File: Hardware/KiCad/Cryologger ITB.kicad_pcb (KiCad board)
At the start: 2 copper layers, 134.6 x 63.5 mm, 18 parts, among them J1 Screw_Terminal_01x02, U1 Adafruit_LSM303AGR, U2 Adafruit_DPS310, U3 Adafruit_Feather_Header, U4 Adafruit_Feather_Header, U5 ROCKBLOCK_9603, U6 Pololu_D36V6, U7 Pololu_D36V6, U8 RockBLOCK_Footprint

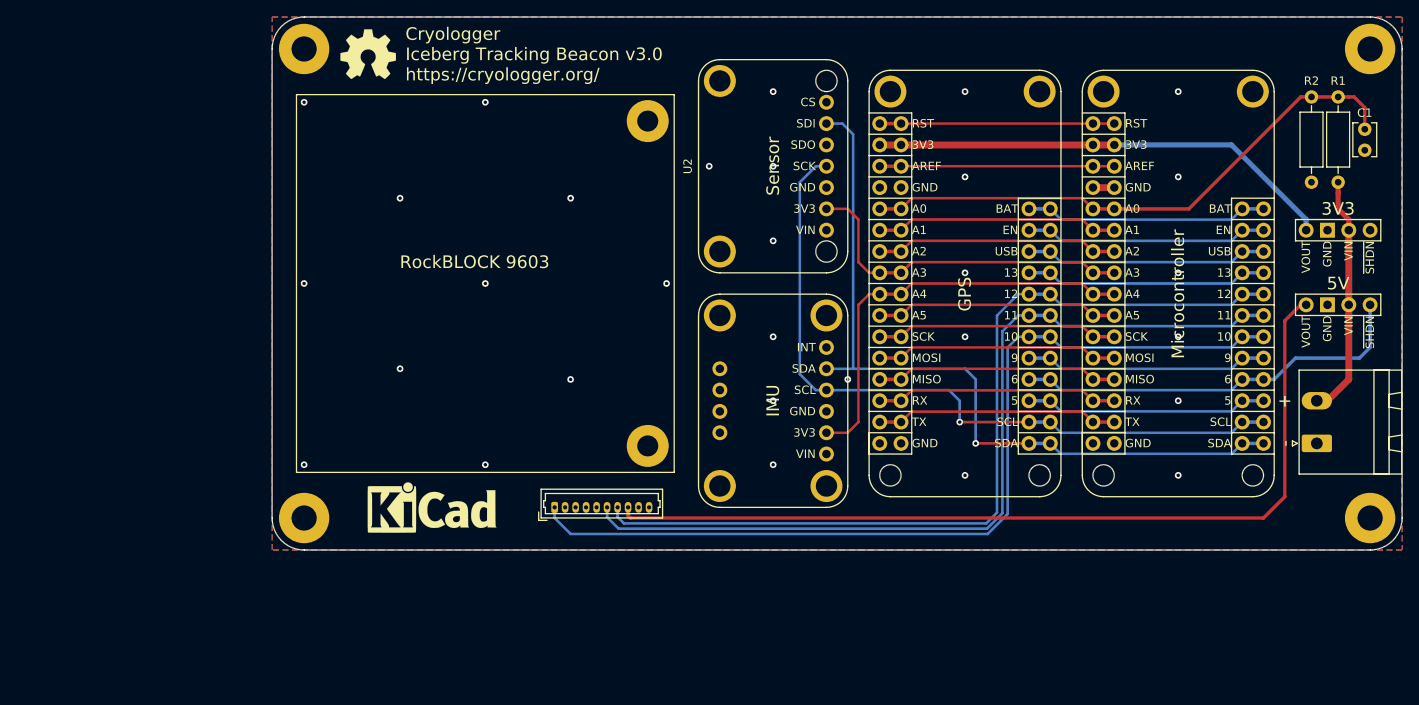
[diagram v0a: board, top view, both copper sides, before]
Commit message: Major changes to KiCad design files
Updated design to v3.1. Began standardization of Cryologger designs to metric measurements. Redid schematic using Cryologger library symbols and footprints. Generated new Gerber design files. Generated current schematic and PCB layout documents. Cleaned up redundant KiCad project files. Removed old 3D printing designs.
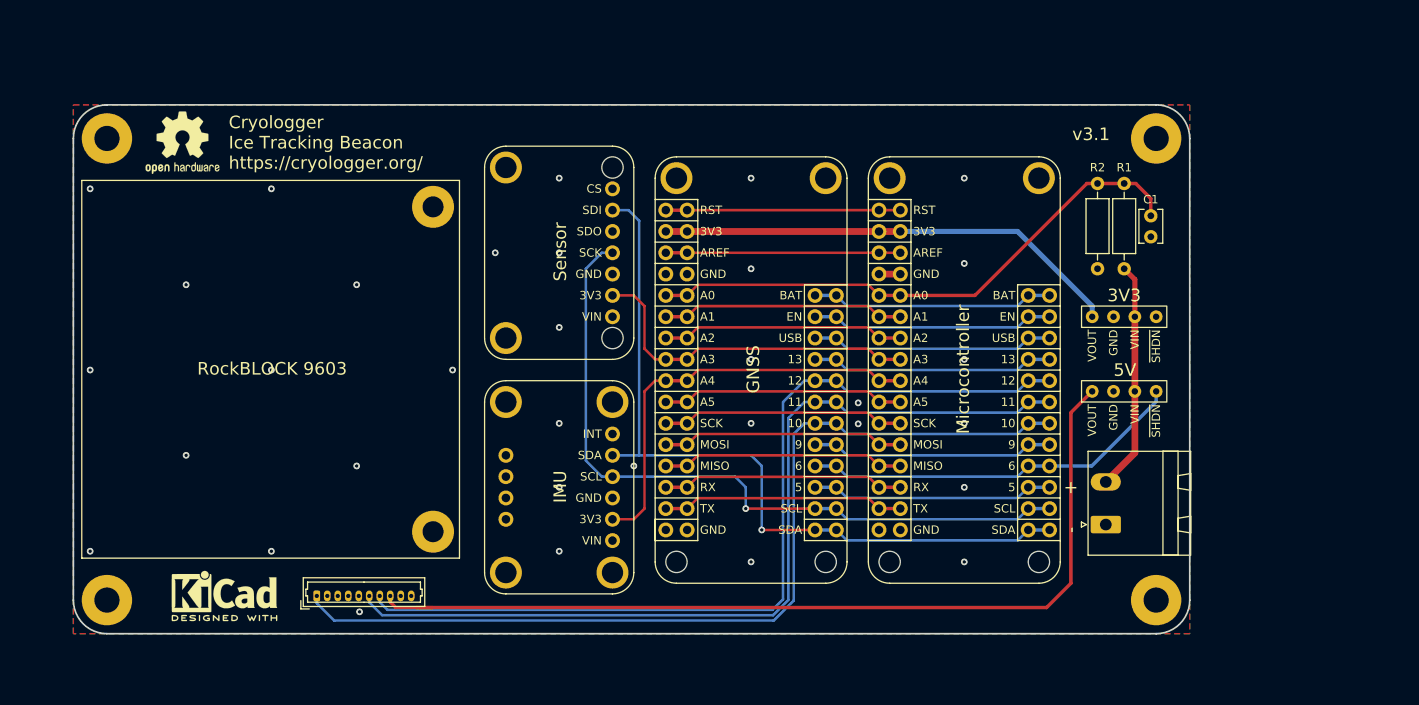
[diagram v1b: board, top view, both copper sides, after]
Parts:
- removed the REF** at (118.1, 54.0)
- removed the REF** at (125.7, 108.0)
- removed U4: Adafruit_Feather_Header, Cryologger:Adafruit_Feather_Header_Double
- removed U5: ROCKBLOCK_9603, Connector_Molex:Molex_PicoBlade_53047-1010_1x10_P1.25mm_Vertical
- removed U7: Pololu_D36V6, Cryologger:Pololu_D36V6_Vertical
- added A2: Adafruit_Feather_Generic, Cryologger:Adafruit_Feather_Header_Double, F.Cu at (163.7, 91.6)
- added A3: Adafruit_Feather_M0_Basic_Proto, Cryologger:Adafruit_Feather_Header_Double, F.Cu at (189.1, 91.6)
- added REF**: OSHW-Logo2_9.8x8mm_SilkScreen, Symbol:OSHW-Logo2_9.8x8mm_SilkScreen, F.Cu at (96.0, 64.5)
- added REF**: KiCad-Logo2_5mm_SilkScreen, Symbol:KiCad-Logo2_5mm_SilkScreen, F.Cu at (101.0, 118.5)
- added U9: Pololu_D36V6x, Cryologger:Pololu_D36V6x, F.Cu at (208.2, 86.5)
- R1: value R_US -> 10MΩ
- R2: value R_US -> 1MΩ
- U2: value Adafruit_DPS310 -> Pololu_D36V6x; footprint Cryologger:Adafruit_DPS310 -> Cryologger:Pololu_D36V6x
- U3: value Adafruit_Feather_Header -> ~; footprint Cryologger:Adafruit_Feather_Header_Double -> Connector_Molex:Molex_PicoBlade_53047-1010_1x10_P1.25mm_Vertical
- U6: value Pololu_D36V6 -> Adafruit_BME280; footprint Cryologger:Pololu_D36V6_Vertical -> Cryologger:Adafruit_DPS310
- U8: footprint Cryologger:RockBLOCK_9603_Footprint -> Cryologger:RockBLOCK_9603
- moved U6 92.8 mm to (140.9, 77.6)
- moved U3 85.7 mm to (112.0, 118.5)
- moved U2 50.4 mm to (208.2, 95.4), turned to 0 degrees
- moved H3 27.6 mm to (212.0, 64.0)
- moved U8 27.5 mm to (106.5, 91.5), turned to 0 degrees
- moved R1 27.5 mm to (208.2, 79.5)
- moved U1 27.5 mm to (140.9, 105.6), turned to 0 degrees
- moved R2 27.5 mm to (205.0, 69.4)
- moved C1 27.5 mm to (211.4, 73.2)
- moved H4 27.3 mm to (212.0, 119.0)
- moved J1 26.9 mm to (206.0, 110.0)
- moved H2 25.8 mm to (87.0, 64.0)
- moved H1 25.4 mm to (87.0, 119.0)
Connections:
- C1 pad 1: /A0 -> A0
- H1 pad 1: GND -> unconnected-(H1-Pad1)
- H2 pad 1: GND -> unconnected-(H2-Pad1)
- H3 pad 1: GND -> unconnected-(H3-Pad1)
- H4 pad 1: GND -> unconnected-(H4-Pad1)
- R1 pad 2: /A0 -> A0
- R2 pad 1: /A0 -> A0
- U1 pad 1: (no net) -> unconnected-(U1-5V-Pad1)
- U1 pad 2: /A4 -> A4
- U1 pad 4: /SCL -> SCL
- U1 pad 5: /SDA -> SDA
- U2 pad 1: (no net) -> +5V
- U2 pad 2: /A3 -> GND
- U2 pad 3: GND -> +BATT
- U2 pad 4: /SCL -> D6
- U3 pad 1: /RST -> D10
- U3 pad 10: /A5 -> GND
- U3 pad 2: +3V3 -> unconnected-(U3-CTS-Pad2)
- U3 pad 3: /AREF -> unconnected-(U3-RTC-Pad3)
- U3 pad 4: GND -> unconnected-(U3-NetAv-Pad4)
- U3 pad 5: /A0 -> unconnected-(U3-RI-Pad5)
- U3 pad 6: /A1 -> D11
- U3 pad 7: /A2 -> D12
- U3 pad 8: /A3 -> +5V
- U3 pad 9: /A4 -> unconnected-(U3-LiIon-Pad9)
- U6 pad 1: +3V3 -> unconnected-(U6-5V-Pad1)
- U6 pad 2: GND -> A3
- U6 pad 3: +BATT -> GND
- U6 pad 4: (no net) -> SCL
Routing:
- net D10: track 0.00 -> 111.4 mm
- net +5V: track 0.00 -> 109.0 mm
- net /D10: track 108.9 -> 0.00 mm
- net D12: track 0.00 -> 107.1 mm
- net D11: track 0.00 -> 106.7 mm
- net /5V: track 105.0 -> 0.00 mm
- net /D12: track 104.5 -> 0.00 mm
- net /D11: track 104.2 -> 0.00 mm
- net /SDA: track 93.5 -> 0.00 mm, vias 1 -> 0
- net SDA: track 0.00 -> 92.9 mm, vias 0 -> 1
- net /SCL: track 87.6 -> 0.00 mm, vias 1 -> 0
- net SCL: track 0.00 -> 87.0 mm, vias 0 -> 1
- net /A0: track 67.4 -> 0.00 mm
- net A0: track 0.00 -> 67.2 mm
- net A4: track 0.00 -> 50.4 mm
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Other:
- board size 134.6 x 63.5 mm -> 133 x 63 mm
- net class Default removed
- board text added: "Cryologger Ice Tracking Beacon https://cryologger.org/"
- board text added: "Designed by: Adam Garbo adam@cryologger.org For more information: https://cryologger.org Notes:"
- board text added: "GNSS"
- board text added: "v3.1"
- board text removed: "Beacon:"
- board text removed: "Contact if found: Adam Garbo University of Ottawa Ottawa, Ontario, Canada adam.garbo@uottawa.ca"
- board text removed: "Cryologger Iceberg Tracking Beacon v3.0 https://cryologger.org/"
- board text removed: "GPS"

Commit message: Minor updates to PCB design
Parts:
- moved H1 9.19 mm to (80.4, 125.4)
- moved H2 9.19 mm to (80.4, 70.4)
- moved H3 9.19 mm to (205.4, 70.4)
- moved H4 9.19 mm to (205.4, 125.4)
- moved J1 9.19 mm to (199.4, 116.4)
- moved R2 9.19 mm to (198.4, 75.7)
- moved REF** 9.19 mm to (89.4, 70.9)
- moved REF** 9.19 mm to (94.4, 124.9)
- moved U1 9.19 mm to (134.2, 111.9)
- moved U3 9.19 mm to (105.4, 124.9)
- moved U8 9.19 mm to (99.9, 97.9)
- moved A2 9.19 mm to (157.1, 97.9)
- moved A3 9.19 mm to (182.5, 97.9)
- moved C1 9.19 mm to (204.7, 79.6)
- moved R1 9.19 mm to (201.5, 85.9)
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
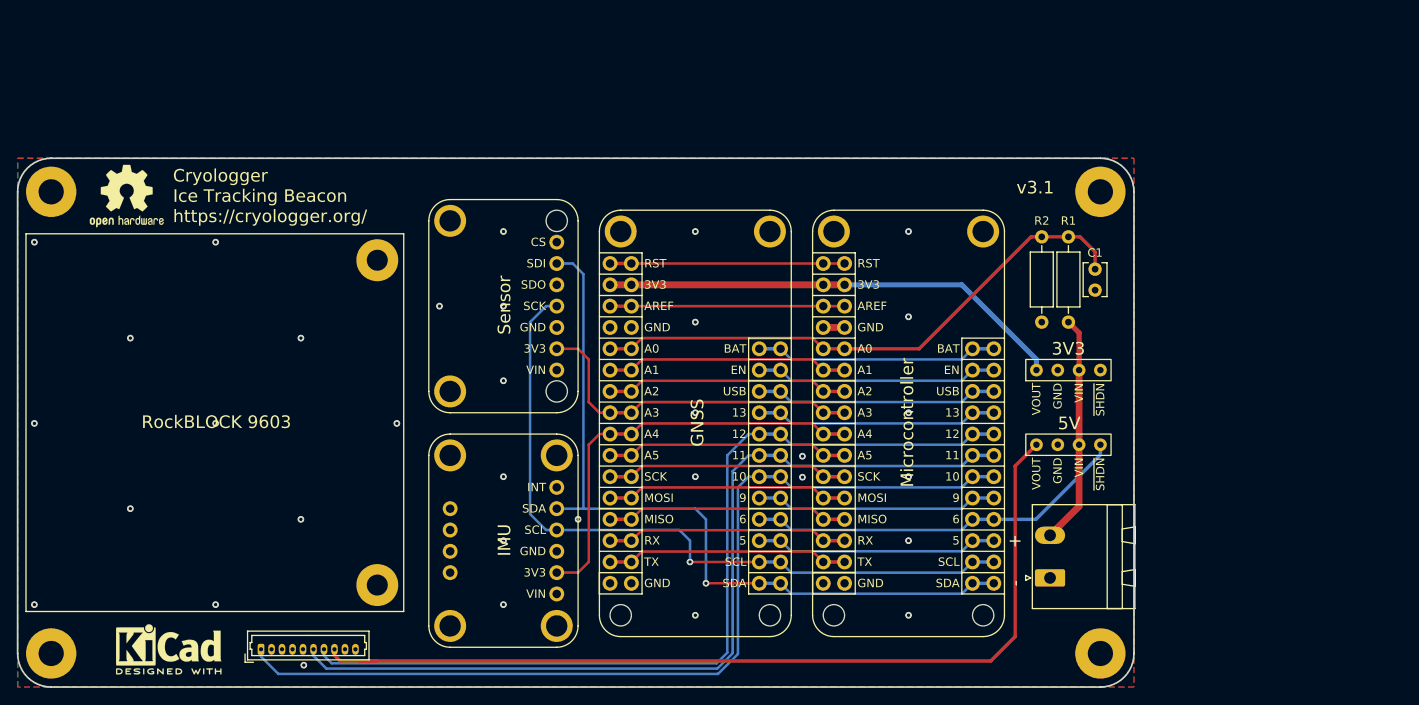
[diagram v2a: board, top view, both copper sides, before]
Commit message: Add N-MOSFET and to control on/off logic of RockBLOCK v3.F
Added a jumper to ensure N-MOSFET is backwards compatible. Updated files to KiCad 8.0.
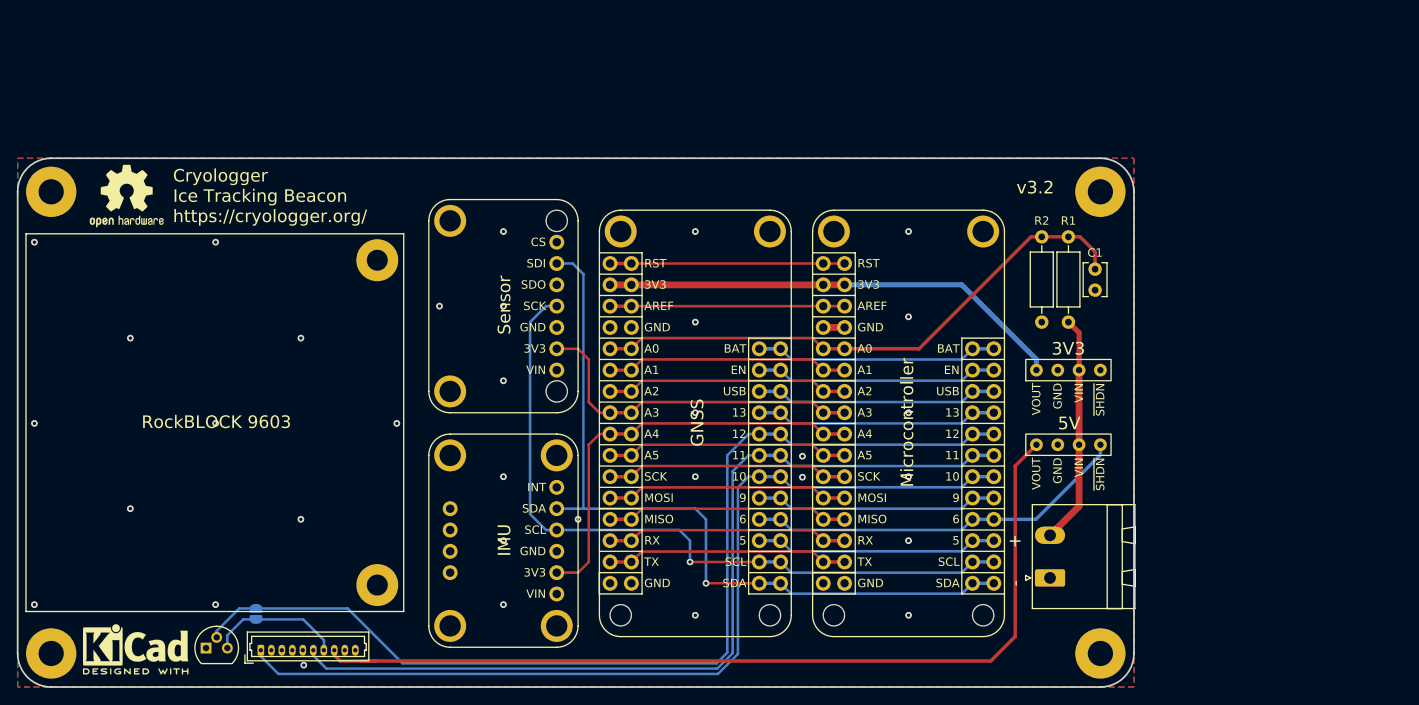
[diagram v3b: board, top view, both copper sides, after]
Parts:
- added JP1: SolderJumper_2_Open, Jumper:SolderJumper-2_P1.3mm_Open_RoundedPad1.0x1.5mm, B.Cu at (104.8, 120.7)
- added Q1: Q_NMOS_SGD, Package_TO_SOT_THT:TO-92, F.Cu at (98.8, 124.7)
- U6: footprint Cryologger:Adafruit_DPS310 -> Cryologger:Adafruit_BME280
- moved REF** 3.93 mm to (90.4, 124.9)
- moved U3 0.11 mm to (105.3, 125.0)
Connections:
- U3 pad 7: D12 -> Net-(JP1-A)
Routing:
- net D12: track 107.1 -> 123.3 mm
- net Net-(JP1-A): track 0.00 -> 15.9 mm
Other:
- board text added: "v3.2"
- board text removed: "v3.1"

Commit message: Add N-MOSFET to PCB to control RockBLOCK v3.F
Updated KiCad files. Added Creative Commons license.
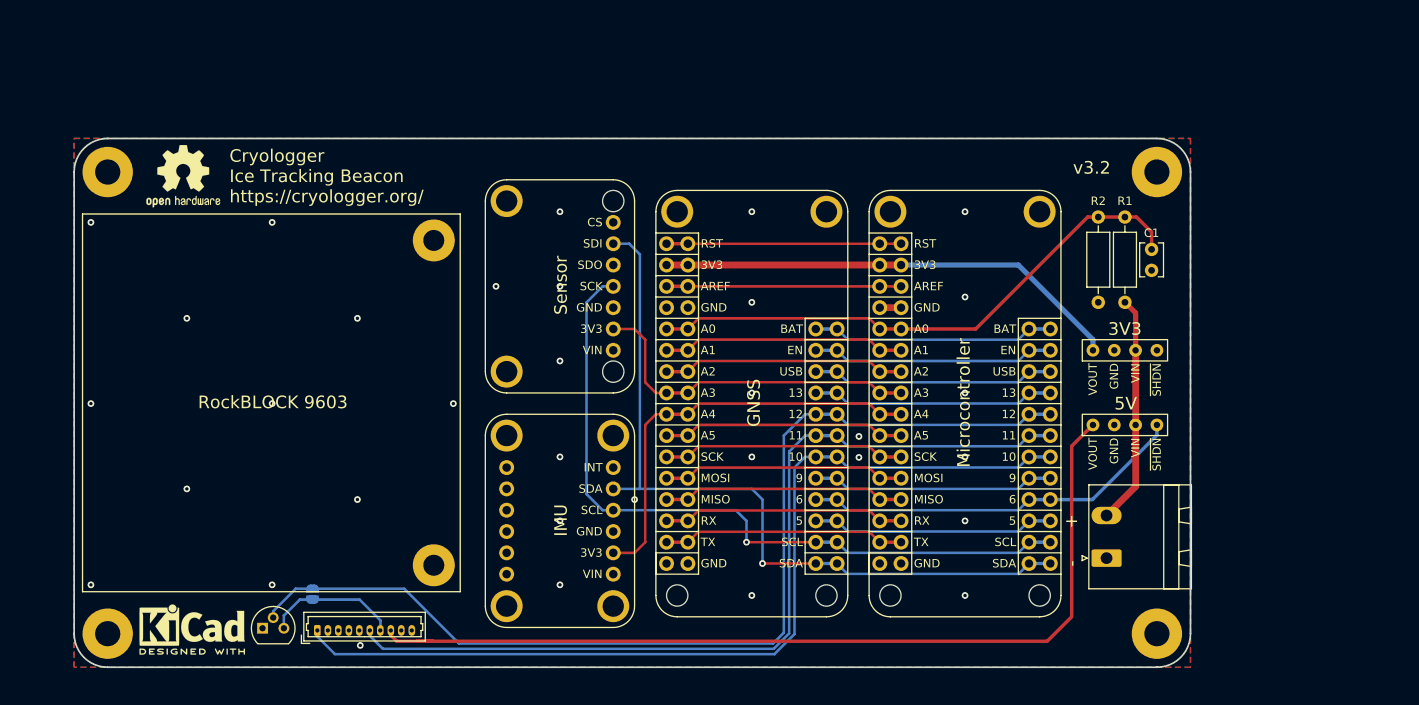
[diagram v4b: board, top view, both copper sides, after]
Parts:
- U1: value Adafruit_LSM303AGR -> Adafruit_LSM6DSOX; footprint Cryologger:Adafruit_LSM303AGR -> Cryologger:Adafruit_LSM6DS0X
- moved H1 7.13 mm to (87.1, 123.0)
- moved H2 7.13 mm to (87.1, 68.0)
- moved H3 7.13 mm to (212.1, 68.0)
- moved H4 7.13 mm to (212.1, 123.0)
- moved J1 7.13 mm to (206.1, 114.0)
- moved JP1 7.13 mm to (111.5, 118.3)
- moved Q1 7.13 mm to (105.5, 122.4)
- moved R2 7.13 mm to (205.1, 73.4)
- moved REF** 7.13 mm to (96.1, 68.5)
- moved REF** 7.13 mm to (97.2, 122.5)
- moved U1 7.13 mm to (141.0, 109.6)
- moved U3 7.13 mm to (112.1, 122.6)
- moved U8 7.13 mm to (106.6, 95.5)
- moved A2 7.13 mm to (163.8, 95.6)
- moved A3 7.13 mm to (189.2, 95.6)
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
